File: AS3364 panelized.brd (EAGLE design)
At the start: 41.9 x 56.5 mm, 117 parts, among them IC1 TL072JD, IC2 TL072JD, IC3 TL072JD, IC4 TL072JD, IC5 TL072JD

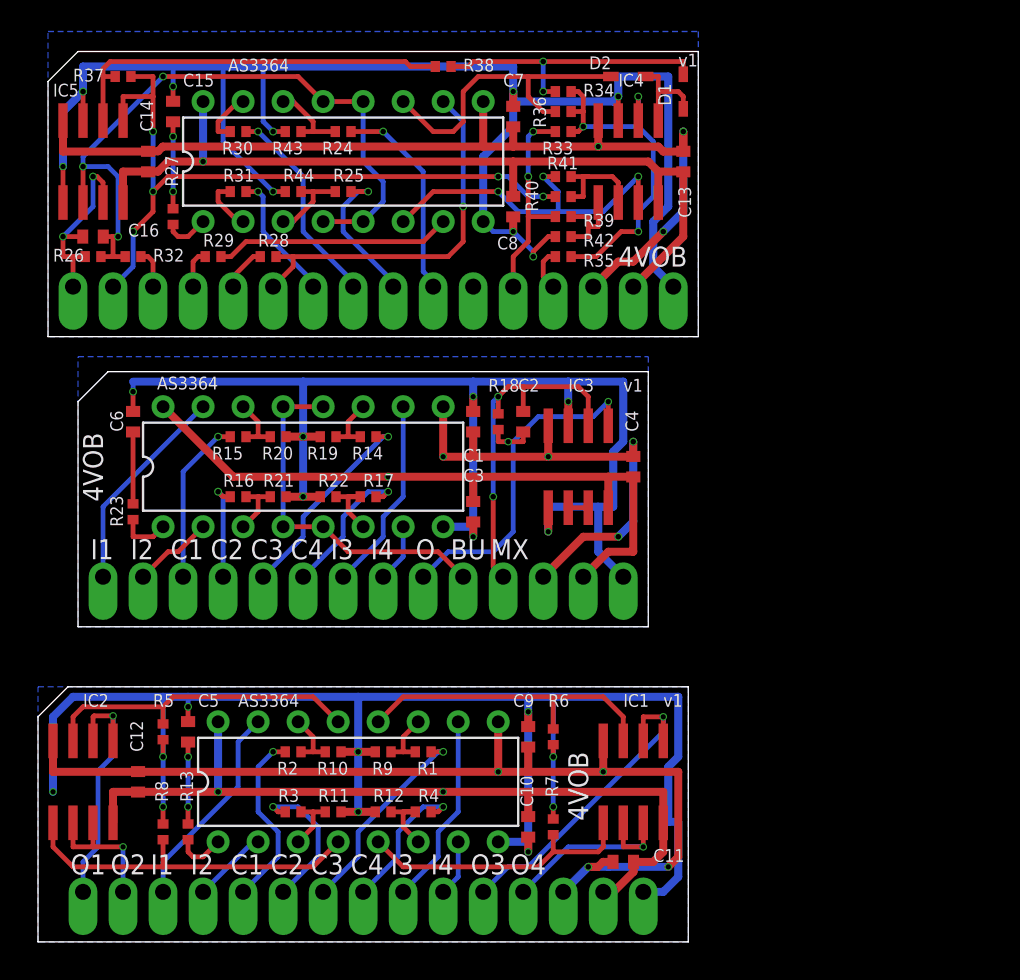
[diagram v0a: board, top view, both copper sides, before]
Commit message: Panelized AS3364
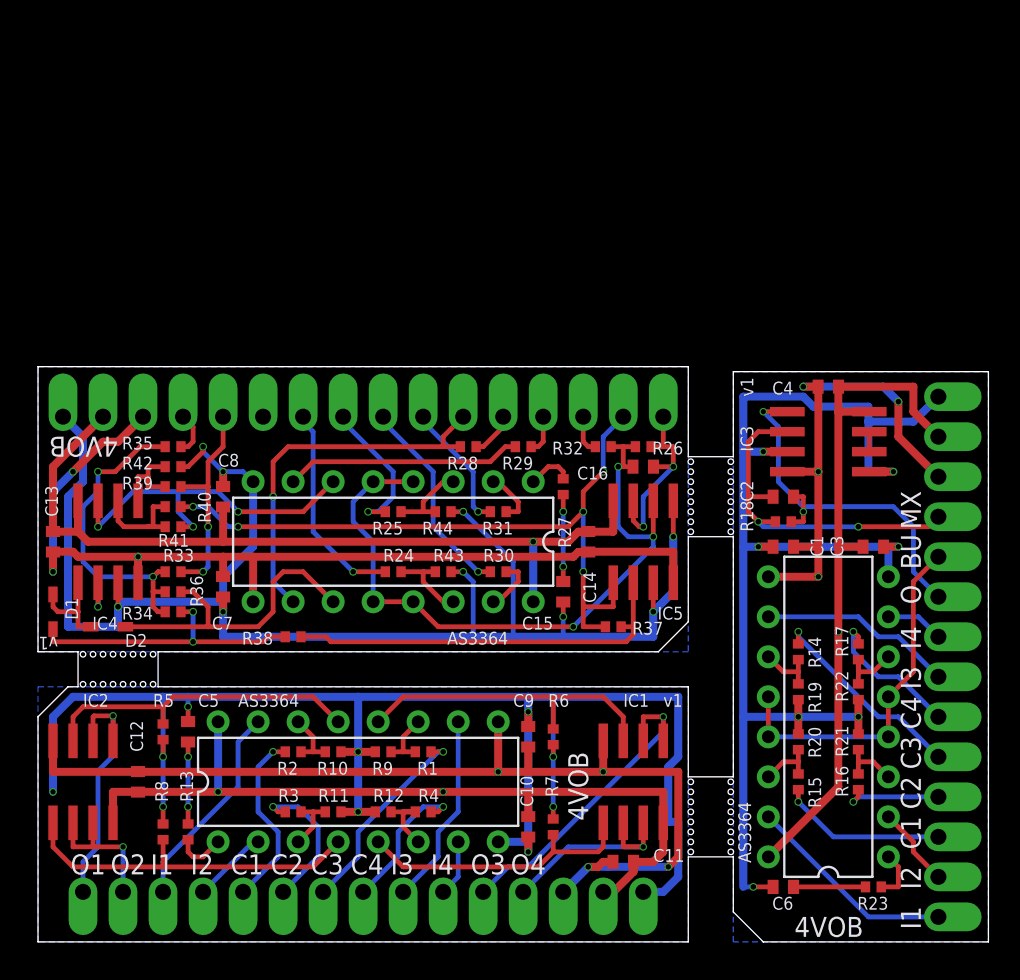
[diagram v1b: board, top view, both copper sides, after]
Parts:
- added U$3: (no value), joakim:XONIK_LOGO_18
- moved IN6 57.2 mm to (57.1, 1.59), turned to 90 degrees
- moved IN7 54.0 mm to (57.1, 4.13), turned to 90 degrees
- moved R23 52.7 mm to (53.0, 3.49), turned to 0 degrees
- moved D1 51.9 mm to (0.95, 21.0), turned to 270 degrees
- moved C6 50.7 mm to (47.3, 3.49), turned to 0 degrees
- moved CV6 50.7 mm to (57.1, 6.67), turned to 90 degrees
- moved D2 48.1 mm to (4.45, 20.0), turned to 180 degrees
- moved CV7 47.5 mm to (57.1, 9.21), turned to 90 degrees
- moved R37 46.8 mm to (36.5, 20.0), turned to 180 degrees
- moved C13 46.7 mm to (0.95, 25.4), turned to 90 degrees
- moved CV5 44.4 mm to (57.1, 11.7), turned to 90 degrees
- moved R16 43.3 mm to (52.1, 10.2), turned to 90 degrees
- moved IC5 42.5 mm to (38.4, 25.4), turned to 0 degrees
- moved R15 41.8 mm to (48.3, 10.2), turned to 90 degrees
- moved CV8 41.3 mm to (57.1, 14.3), turned to 90 degrees
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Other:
- board size 41.9 x 56.5 mm -> 60.3 x 36.5 mm
- board text added: "1"
- board text added: "1C"
- board text added: "2"
- board text added: "2C"
- board text added: "5V"
- board text added: "CV"
- board text added: "IN"
- board text added: "Pulse"
- board text added: "SW"
- board text added: "Sub osc"
- board text added: "TD"
- board text added: "TR"
- board text added: "Wave- shape mixer"

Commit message: Almost finished bom/cpl
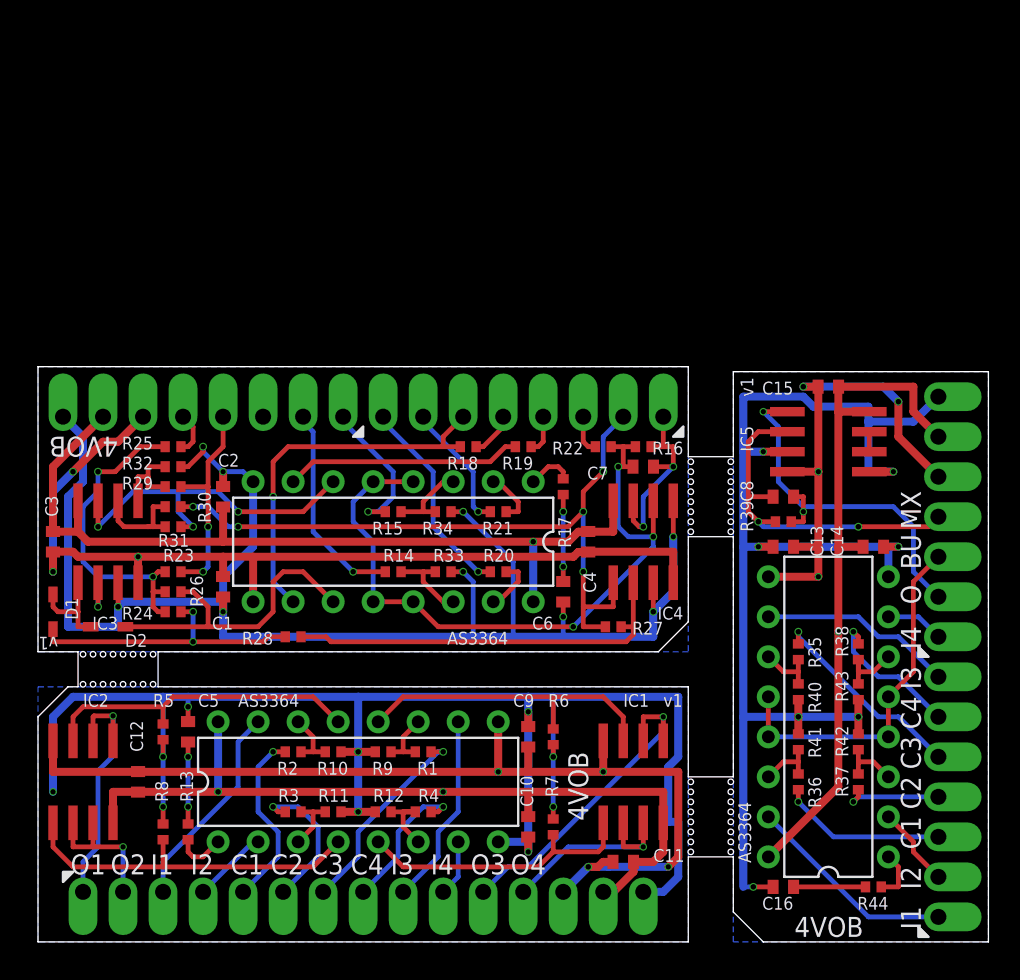
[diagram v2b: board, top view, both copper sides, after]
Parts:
- removed +12V, +12V1, +12V2, -12V, -12V1, -12V2, -5V, BUS, CV1, CV2, CV3, CV4, CV5, CV6, CV7, CV8, GND, GND1, GND2, IN1, IN2, IN3, IN4, IN5, IN6, IN7, IN8, MIX, NC1, OUT, OUT1, OUT2, OUT3, OUT4, OUT5, PAN_CV, PULSE_CV_OUT, PULSE_IN, SAW, SUB1, SUB1_CV, SUB2, SUB2_CV, TRI, TRI_DIRECT: (no value), joakim:SIP-PIN01-1J
- added SV1: (no value), joakim:SIP-PIN15-1J
- added SV2, SV3: (no value), joakim:SIP-PIN08-1J
- added U$4, U$5: MA07-1JP, joakim:SIP-PIN07-1J
- C15: value 5nF -> 100nF
- C16: value 33pF -> 5nF
- C2: value 33pF -> 100nF
- C7, C8: value 100nF -> 33pF
- R16: value 33k -> 47k
- R17: value 33k -> 100R
- R19, R20, R21, R22: value 22k -> 47k
- R23, R27: value 100R -> 25k
- R24: value 33k -> 20k
- R25: value 33k -> 50k
- R26, R31, R32: value 47k -> 20k
- R28: value 47k -> 10k
- R29, R30: value 47k -> 25k
- R33, R40: value 25k -> 22k
- R34, R41, R42: value 20k -> 22k
- R35: value 50k -> 33k
- R36: value 20k -> 33k
- R37: value 25k -> 33k
- R38: value 10k -> 33k
- R39: value 25k -> 47k
- R44: value 22k -> 100R
- moved C3 52.1 mm to (0.95, 25.4), turned to 90 degrees
- moved R23 48.7 mm to (8.57, 23.5), turned to 180 degrees
- moved R42 46.9 mm to (52.1, 12.7), turned to 270 degrees
- moved C13 46.4 mm to (47.3, 25.1), turned to 180 degrees
- moved IC3 46.2 mm to (4.45, 25.4), turned to 0 degrees
- moved R41 42.0 mm to (48.3, 12.7), turned to 270 degrees
- moved R35 41.8 mm to (48.3, 18.4), turned to 270 degrees
- moved R36 41.5 mm to (48.3, 10.2), turned to 90 degrees
- moved R40 41.4 mm to (48.3, 15.9), turned to 90 degrees
- moved U$2 38.9 mm to (13.3, 27.2), turned to 180 degrees
- moved U$3 38.9 mm to (52.0, 23.5), turned to 270 degrees
- moved R39 38.8 mm to (47.3, 26.7), turned to 0 degrees
- moved R44 36.2 mm to (53.0, 3.49), turned to 0 degrees
- moved R38 35.9 mm to (52.1, 18.4), turned to 270 degrees
- moved C1 35.7 mm to (11.7, 22.5), turned to 270 degrees
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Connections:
- net +12V: now also SV1.14; no longer +12V.1
- net +12V1: now also C2.2, IC4.8, SV3.7; no longer +12V1.1
- net +12V2: now also C15.2, U$4.6; no longer +12V2.1, C13.2, C8.2, IC4.8
- net -12V: now also SV1.13; no longer -12V.1
- net -12V1: now also C3.1, IC4.4, SV3.6; no longer -12V1.1
- net -12V2: now also C15.1, U$4.5; no longer -12V2.1, C14.1, C7.1, IC4.4
- net -5V: now also R25.1, SV3.5; no longer -5V.1, R35.1
- net BUS: now also DA3.12, DA3.13, DA3.4, DA3.5, U$4.3; no longer BUS.1, DA1.12, DA1.13, DA1.4, DA1.5
- net CV1: now also SV1.5; no longer CV1.1
- net CV2: now also SV1.6; no longer CV2.1
- net CV2_IN1: now also DA3.3, R37.2, R42.2; no longer DA1.3, R16.2, R21.2
- net CV3: now also SV1.7; no longer CV3.1
- net CV4: now also SV1.8; no longer CV4.1
- net CV5: now also R36.1, U$5.3; no longer CV6.1, R15.1
- net CV6: now also R35.1, U$5.5; no longer CV5.1, R14.1
- net CV7: now also R38.1, U$5.6; no longer CV8.1, R17.1
- net CV8: now also R37.1, U$5.4; no longer CV7.1, R16.1
- net GND: now also SV1.15; no longer GND.1
- net GND1: now also C2.1, IC4.3, IC4.5, R32.1, R33.1, R34.1, SV3.8; no longer C3.1, GND1.1, IC3.5, R19.1, R20.1, R21.1, R22.1
- net GND2: now also C13.2, C14.1, C16.1, R40.1, R41.1, U$4.7; no longer C15.1, C7.2, C8.1, GND2.1, IC4.3, R44.1
- net IN1: now also SV1.3; no longer IN1.1
- net IN2: now also SV1.4; no longer IN2.1
- net IN3: now also SV1.9; no longer IN3.1
- net IN4: now also SV1.10; no longer IN4.1
- net IN5: now also DA3.10, U$5.7; no longer DA1.10, IN5.1
- net IN6: now also DA3.7, U$4.1; no longer DA1.7, IN8.1
- net IN7: now also DA3.2, U$5.2; no longer DA1.2, IN7.1
- net IN8: now also DA3.15, U$5.1; no longer DA1.15, IN6.1
- net MIX: now also C8.1, IC5.2, R39.1, U$4.4; no longer C2.1, IC3.2, MIX.1, R18.1
- net MIX_BUS: now also C7.2, DA1.12, DA1.13, DA1.4, DA1.5, IC4.6, R16.2, R22.1; no longer C16.2, DA3.12, DA3.13, DA3.4, DA3.5, IC5.6, R26.2, R32.1
- net N$1: now also R17.2; no longer R23.2
- net N$15: now also IC3.6, R30.2, R31.1; no longer C15.2, R27.1
- net N$16: now also DA3.6, R38.2, R43.2; no longer IC4.2, R33.2, R34.1, R35.2, R36.1
- net N$17: now also DA3.11, R35.2, R40.2; no longer IC4.5, R39.2, R42.2
- net N$18: now also IC4.2, R27.1, R28.2; no longer IC4.6, R40.2, R41.1
- net N$19: now also D1.2, R24.2, R28.1; no longer IC5.2, R37.1, R38.2
- net N$20: now also DA3.14, R36.2, R41.2; no longer D1.1, D2.2, IC4.1
- net N$22: now also C16.2, R44.1; no longer D1.2, R34.2, R38.1
- net N$3: now also C6.2, R17.1; no longer DA1.6, R17.2, R22.2
- net N$5: now also IC3.5, R29.2, R32.2; no longer DA1.11, R14.2, R19.2
- net N$7: now also D1.1, D2.2, IC3.1; no longer DA1.14, R15.2, R20.2
- net N$8: now also IC3.2, R23.2, R24.1, R25.2, R26.1; no longer C6.2, R23.1
- net N$9: now also R44.2; no longer R27.2
- net NC1: now also IC5.6, IC5.7; no longer IC3.6, IC3.7
- net OUT: now also C7.1, IC4.7, R16.1, SV2.1; no longer C2.2, IC3.1, OUT.1, R18.2
- net OUT1: now also SV1.1; no longer OUT1.1
- net OUT2: now also SV1.2; no longer OUT2.1
- net OUT3: now also SV1.11; no longer OUT3.1
- net OUT4: now also SV1.12; no longer OUT4.1
- net OUT5: now also C8.2, IC5.1, R39.2, U$4.2; no longer C16.1, IC5.7, OUT5.1, R26.1
- net PAN_CV: now also R23.1, R29.1, SV3.4; no longer PAN_CV.1, R33.1, R39.1
- net PULSE_CV: now also IC4.1, R27.2, R30.1, SV2.2; no longer IC5.1, PULSE_CV_OUT.1, R37.2, R40.1
- net PULSE_IN: now also R22.2, SV2.3; no longer PULSE_IN.1, R32.2
- net SAW: now also R19.1, SV2.4; no longer R29.1, SAW.1
- net SAW_CV: now also DA1.6, IC3.7, R31.2; no longer DA3.6, IC4.7, R41.2
- net SAW_IN: now also DA1.7, R19.2; no longer DA3.7, R29.2
- net SUB1: now also R20.1, SV2.8; no longer R30.1, SUB1.1
- net SUB1_CV: now also R14.1, SV3.2; no longer R24.1, SUB1_CV.1
- net SUB1_CV_IN: now also DA1.14, R14.2, R33.2; no longer DA3.14, R24.2, R43.2
- net SUB1_IN: now also DA1.15, R20.2; no longer DA3.15, R30.2
- net SUB2: now also R21.1, SV2.7; no longer R31.1, SUB2.1
- net SUB2_CV: now also R15.1, SV3.1; no longer R25.1, SUB2_CV.1
- net SUB2_CV_IN: now also DA1.3, R15.2, R34.2; no longer DA3.3, R25.2, R44.2
- net SUB2_IN: now also DA1.2, R21.2; no longer DA3.2, R31.2
- net TRI: now also R18.1, SV2.5; no longer R28.1, TRI.1
- net TRI_CV: now also DA1.11, R26.2; no longer DA3.11, R36.2
- net TRI_IN: now also DA1.10, R18.2, SV2.6; no longer DA3.10, R28.2, TRI_DIRECT.1
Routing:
- net -12V2: track 62.7 -> 32.0 mm, vias 3 -> 4
- net -12V1: track 32.0 -> 62.7 mm, vias 4 -> 3
- net GND2: track 102.3 -> 81.6 mm, vias 9 -> 7
- net GND1: track 81.6 -> 102.3 mm, vias 7 -> 9
- net N$8: track 4.56 -> 23.8 mm, vias 0 -> 3
- net N$16: track 23.8 -> 4.61 mm, vias 3 -> 0
- net N$18: track 6.46 -> 25.5 mm
- net N$22: track 18.4 -> 4.56 mm, vias 2 -> 0
- net OUT5: track 12.5 -> 24.5 mm
- net OUT: track 24.5 -> 12.5 mm
- net +12V2: track 54.7 -> 43.8 mm
- net +12V1: track 43.8 -> 54.7 mm
- net N$19: track 25.5 -> 18.4 mm, vias 0 -> 2
- net N$7: track 3.84 -> 6.10 mm
- net N$20: track 6.10 -> 3.84 mm
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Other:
- board text added: "-5V"
- board text removed: "5V"
